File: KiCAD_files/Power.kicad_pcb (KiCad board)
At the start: 4 copper layers, 100 x 100 mm, 206 parts, among them J1 Conn_01x01, J10 Conn_01x01, J101 2604-1102, J102 2604-1102, J103 2604-1102, J104 Conn_01x01, J105 Conn_01x01, J106 Conn_01x01, J107 Conn_01x01, J108 Conn_01x01, J109 Conn_01x01, J110 Conn_01x01, J111 Conn_01x01, J112 Conn_01x01, J113 Conn_01x01, J114 Conn_01x01, J115 Conn_01x01, J116 Conn_01x01, J117 2604-1102, J118 2604-1102, J2 Conn_01x01, J201 Conn_01x01, J202 Conn_01x01, J203 Conn_01x01, J204 Conn_01x01, J205 Conn_01x01, J206 Conn_01x01, J207 Conn_01x01, J208 Conn_01x01, J209 Conn_01x01, J210 Conn_01x01, J3 Conn_01x01, J4 Conn_01x01, J5 Conn_01x01, J6 Conn_01x01, J7 Conn_01x01, J8 Conn_01x01, J9 Conn_01x01, Q1 IPD200N15N3, Q2 IPD200N15N3, Q201 IPD200N15N3, Q202 IPD200N15N3, Q203 IPD200N15N3, Q3 IPD200N15N3, U1 AMC1100DUB, U101 AMC1311, U102 OPA316, U103 OPA316, U104 +-20A, U2 ACS730xLCTR-20AB, U201 AMC1100DUB, U202 ACS730xLCTR-20AB, U203 UCC21222DR, U204 OPA316, U205 OPA316, U206 SFH617A-2X009T, U3 UCC21222DR, U4 OPA316, U5 OPA316, U6 SFH617A-2X009T

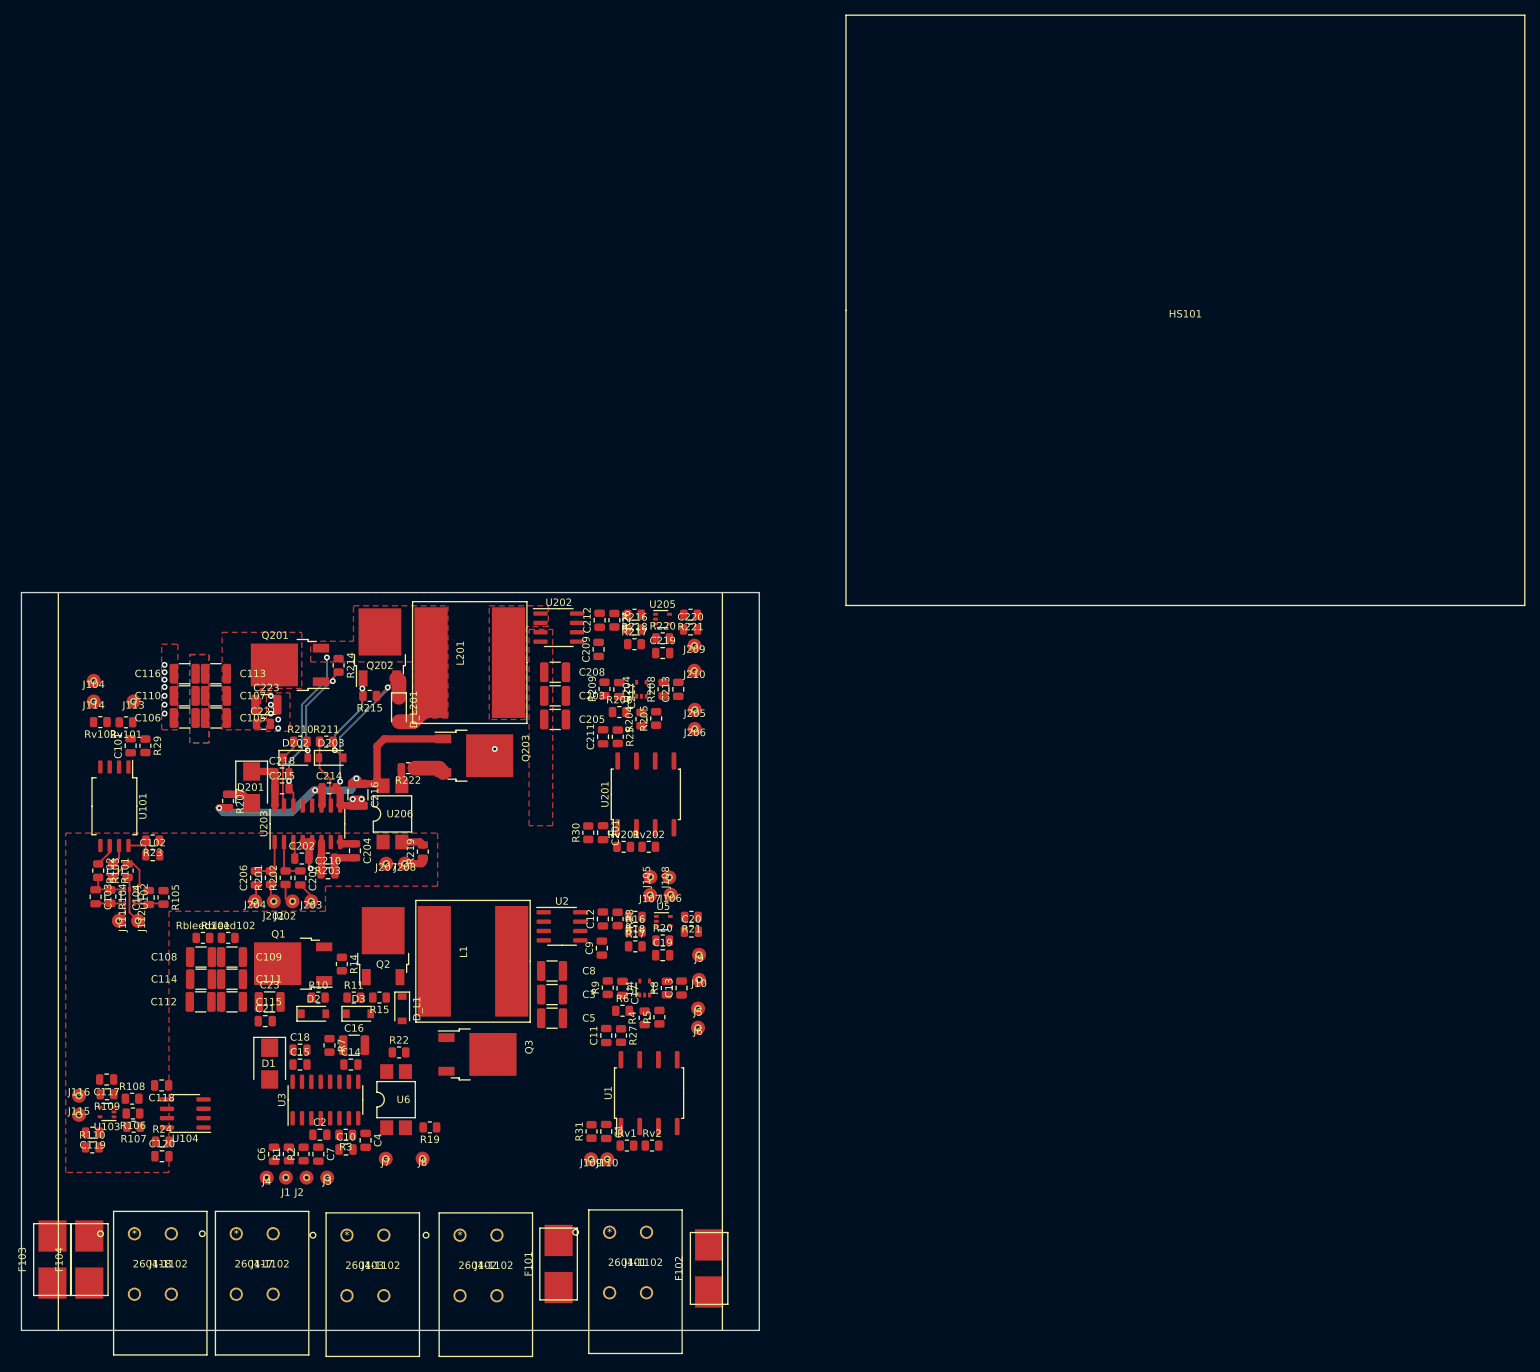
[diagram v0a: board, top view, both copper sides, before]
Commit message: [Power] Finished routing all the tracks, no more rastnet, ready for refining
Former-commit-id: c85419efed005dbd6b325ef0aef7156952f8cebe
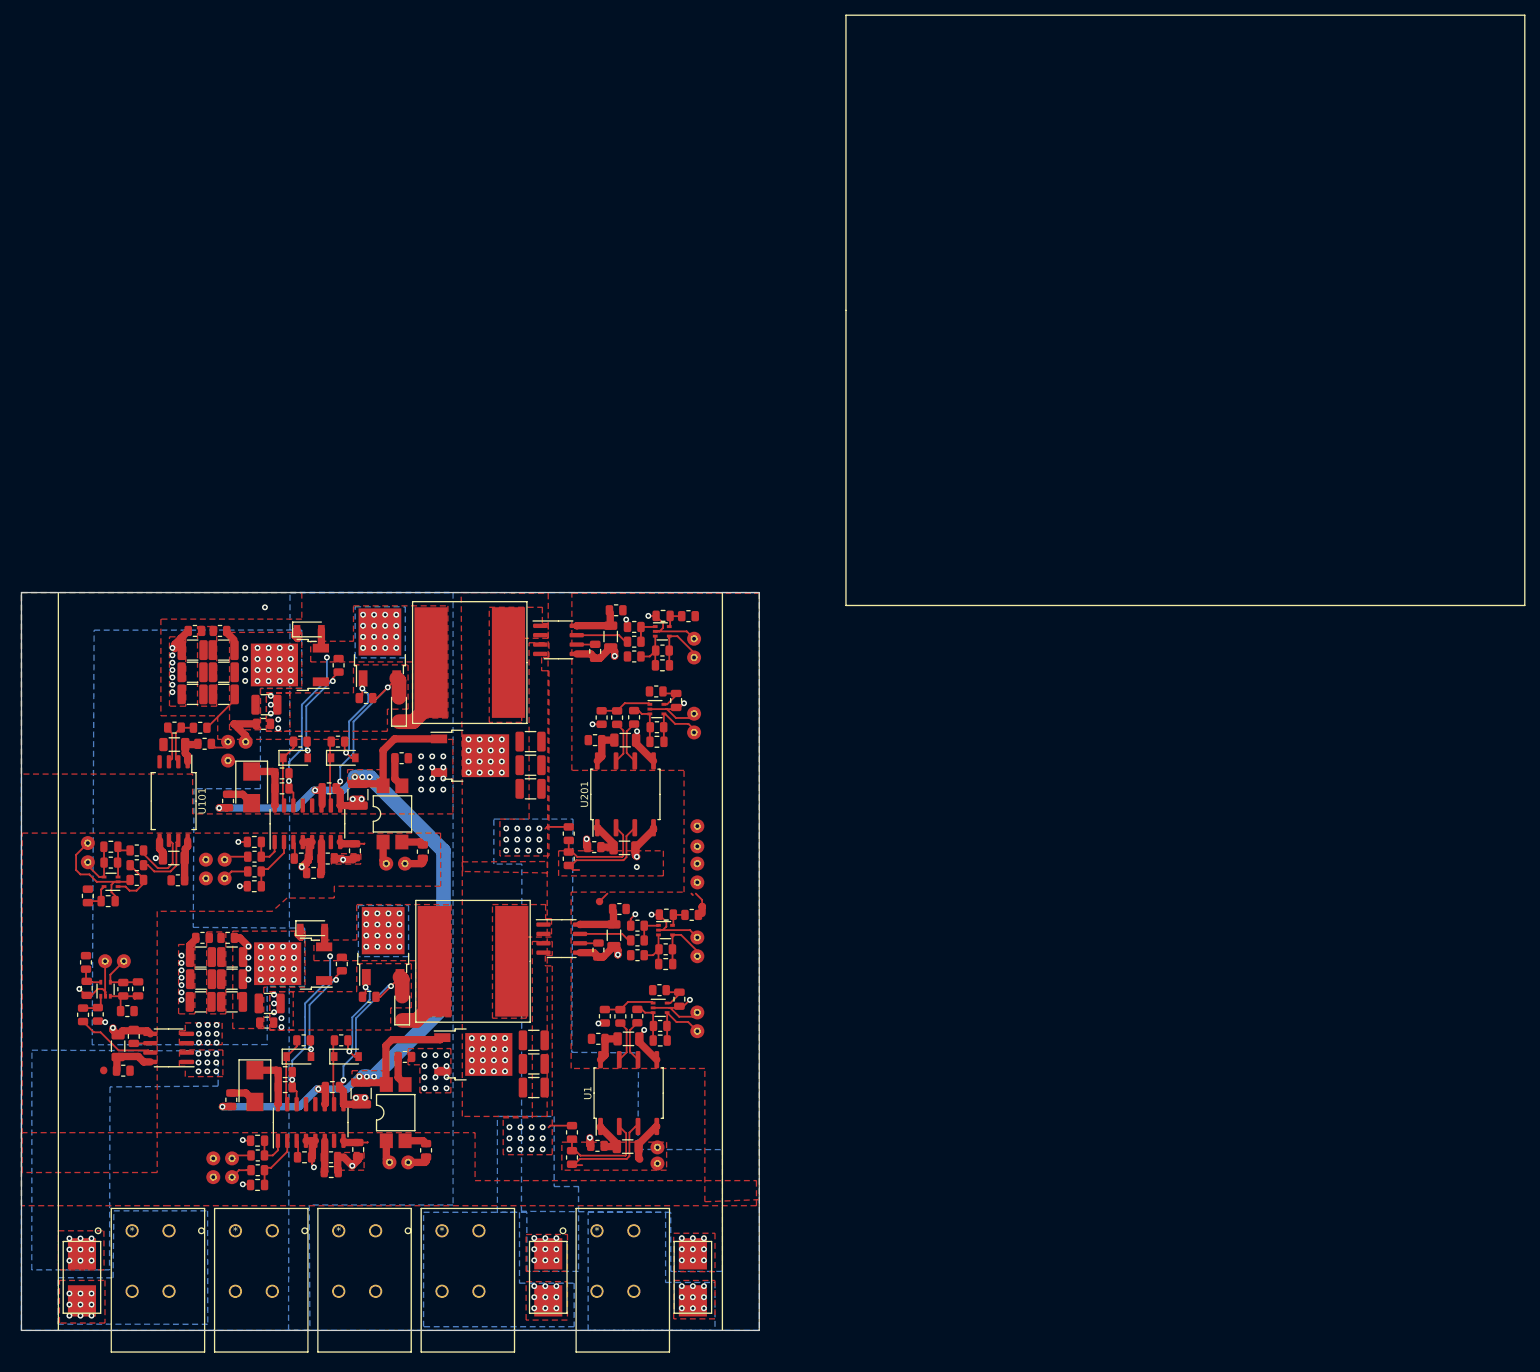
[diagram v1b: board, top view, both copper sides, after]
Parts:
- removed F104: 8A, Footprints:Fuse_holder_omni_blok
- added D_L202: STTH1002CB, Diode_SMD:D_SOD-123, F.Cu at (81.0, 47.0)
- added D_L3: STTH1002CB, Diode_SMD:D_SOD-123, F.Cu at (81.4, 87.5)
- added Rbleed1: 1M, Resistor_SMD:R_0805_2012Metric, F.Cu at (68.9, 47.2)
- added Rbleed2: 1M, Resistor_SMD:R_0805_2012Metric, F.Cu at (65.5, 47.2)
- C1, C101, C102, C11, C12, C120, C201, C211, C212: footprint Capacitor_SMD:C_0805_2012Metric -> Capacitor_SMD:C_1206_3216Metric
- R106, R109, R16, R20, R216, R220: value 62k -> 5.9k
- R107, R108, R17, R18, R217, R218: value 43k -> 20k
- U1, U201: footprint Package_SO:SOP-8_6.62x9.15mm_P2.54mm -> Footprints:SOP-8_6.62x9.15mm_P2.54mm
- U101: footprint Package_SO:SOIC-8_7.5x5.85mm_P1.27mm -> Footprints:SOIC-8_7.5x5.85mm_P1.27mm
- moved C108 41.6 mm to (65.2, 49.8)
- moved C109 41.6 mm to (69.4, 49.8)
- moved C113 38.5 mm to (70.6, 91.4)
- moved C116 38.5 mm to (66.3, 91.4)
- moved R110 25.1 mm to (50.8, 92.1), turned to -90 degrees
- moved J115 21.7 mm to (55.9, 92.0), turned to 90 degrees
- moved J104 20.0 mm to (70.0, 62.2)
- moved J114 19.9 mm to (70.0, 64.8)
- moved C119 19.6 mm to (50.9, 95.6), turned to -90 degrees
- moved J116 18.6 mm to (53.3, 92.0), turned to 90 degrees
- moved U103 16.6 mm to (53.4, 95.8), turned to 90 degrees
- moved C208 16.1 mm to (111.0, 68.6), turned to 180 degrees
- moved J113 16.1 mm to (72.4, 62.2)
- moved C120 16.1 mm to (55.1, 103.5), turned to -90 degrees
- moved C8 16.0 mm to (111.4, 109.1), turned to 180 degrees
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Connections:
- net /Power Leg 1/HRTIM1_CHB1 renamed /Power Leg 1/HRTIM1_CH1
- net /Power Leg 1/HRTIM1_CHB2 renamed /Power Leg 1/HRTIM1_CH2
- net /Power Leg 1/IILow1 renamed /Power Leg 1/IILow
- net /Power Leg 1/VILow1+ renamed /Power Leg 1/VILow+
- net /Power Leg 1/VILow1_op renamed /Power Leg 1/VILow_op
- net /Power Leg 2/HRTIM1_CHB1 renamed /Power Leg 2/HRTIM1_CH1
- net /Power Leg 2/HRTIM1_CHB2 renamed /Power Leg 2/HRTIM1_CH2
- net /Power Leg 2/IILow1 renamed /Power Leg 2/IILow
- net /Power Leg 2/VILow1+ renamed /Power Leg 2/VILow+
- net /Power Leg 2/VILow1_op renamed /Power Leg 2/VILow_op
- C105 pad 1: /Power Leg 1/V_High -> /V_High
- C107 pad 1: /Power Leg 1/V_High -> /V_High
- C109 pad 1: /Power Leg 1/V_High -> /V_High
- C111 pad 1: /Power Leg 1/V_High -> /V_High
- C111 pad 2: Net-(C105-Pad2) -> Net-(C111-Pad2)
- C112 pad 1: Net-(C105-Pad2) -> Net-(C111-Pad2)
- C113 pad 1: /Power Leg 1/V_High -> /V_High
- C113 pad 2: Net-(C105-Pad2) -> Net-(C111-Pad2)
- C114 pad 1: Net-(C105-Pad2) -> Net-(C111-Pad2)
- C115 pad 1: /Power Leg 1/V_High -> /V_High
- C115 pad 2: Net-(C105-Pad2) -> Net-(C111-Pad2)
- C116 pad 1: Net-(C105-Pad2) -> Net-(C111-Pad2)
- C21 pad 1: /Power Leg 1/V_High -> /V_High
- C221 pad 1: /Power Leg 1/V_High -> /V_High
- C223 pad 1: /Power Leg 1/V_High -> /V_High
- C23 pad 1: /Power Leg 1/V_High -> /V_High
- D_L1 pad 1: GNDREF -> /Power Leg 2/SW_Node
- D_L1 pad 2: /Power Leg 2/SW_Node -> GNDREF
- D_L201 pad 1: GNDREF -> /Power Leg 1/SW_Node
- D_L201 pad 2: /Power Leg 1/SW_Node -> GNDREF
- J113 pad 1: /VI_High -> /V_High
- Q1 pad 2: /Power Leg 1/V_High -> /V_High
- Q201 pad 2: /Power Leg 1/V_High -> /V_High
- R107 pad 1: VRef -> +5VD
- R17 pad 1: VRef -> +5VD
- R217 pad 1: VRef -> +5VD
- Rbleed101 pad 1: /Power Leg 1/V_High -> /V_High
- Rbleed101 pad 2: Net-(C105-Pad2) -> Net-(C111-Pad2)
- Rbleed102 pad 1: Net-(C105-Pad2) -> Net-(C111-Pad2)
- Rv101 pad 1: /Power Leg 1/V_High -> /V_High
- U104 pad 3: /Power Leg 1/V_High -> /V_High
- U104 pad 4: /Power Leg 1/V_High -> /V_High
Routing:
- net DGND: track 24.4 -> 140.6 mm, vias 1 -> 22
- net +12V: track 45.3 -> 136.2 mm, vias 3 -> 10
- net VRef: track 0.00 -> 73.6 mm, vias 0 -> 2
- net +5V: track 0.00 -> 67.7 mm, vias 0 -> 2
- net NGND: track 0.00 -> 39.4 mm, vias 1 -> 34
- net GNDREF: track 34.1 -> 72.7 mm, vias 16 -> 57
- net /Power Leg 2/SW_Node: track 0.00 -> 37.0 mm, vias 0 -> 18
- net /V_High: track 0.00 -> 20.1 mm, vias 0 -> 49
- net Net-(D2-Pad2): track 0.00 -> 16.5 mm, vias 0 -> 2
- net Net-(D3-Pad2): track 0.00 -> 16.1 mm, vias 0 -> 2
- net /Power Leg 1/VILow+: track 0.00 -> 13.5 mm
- net /Power Leg 2/VILow+: track 0.00 -> 13.5 mm
- net +5VD: track 4.41 -> 17.4 mm
- net /IIHigh: track 0.00 -> 10.9 mm
- net /Power Leg 2/IILow1_op: track 0.00 -> 9.71 mm
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- added copper zone on F.Cu, net +12V
- added copper zone on F.Cu, net +5VD
- added copper zone on B.Cu, net /Power Leg 1/SW_Node
- added copper zone on B.Cu, net /Power Leg 2/SW_Node
- added copper zone on F.Cu, net /Power Leg 2/SW_Node
- added copper zone on B.Cu, net /V1_Low
- added copper zone on B.Cu, net /V2_Low
- added copper zone on F.Cu, net /V2_Low
- added copper zone on B.Cu, net /VI_High
- added copper zone on F.Cu, net /VI_High
- added copper zone on B.Cu, net /V_High
- added copper zone on F.Cu, net /V_High
- added copper zone on In1.Cu, net DGND
- added copper zone on B.Cu, net GNDREF
- added copper zone on In2.Cu, net GNDREF
- added copper zone on B.Cu, net NGND
- added copper zone on F.Cu, net NGND
- added copper zone on In2.Cu, net NGND
- added copper zone on F.Cu, net Net-(C111-Pad2)
- added copper zone on B.Cu, net Net-(F101-Pad2)
- added copper zone on F.Cu, net Net-(F101-Pad2)
- added copper zone on B.Cu, net Net-(F102-Pad2)
- added copper zone on F.Cu, net Net-(F102-Pad2)
- added copper zone on B.Cu, net Net-(F103-Pad2)
- added copper zone on F.Cu, net Net-(F103-Pad2)
- added copper zone on F.Cu, net Net-(L1-Pad1)
- removed copper zone on F.Cu, net /Power Leg 1/V_High
- removed copper zone on B.Cu, net Net-(C105-Pad2)

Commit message: Supressed backup files
Former-commit-id: af6064aba0445a9773bde6e74b771947025d2895
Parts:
- added H1: MountingHole, MountingHole:MountingHole_3.2mm_M3, F.Cu at (130.6, 114.2)
- added H2: MountingHole, MountingHole:MountingHole_3.2mm_M3, F.Cu at (100.3, 114.0)
- added H3: MountingHole, MountingHole:MountingHole_3.2mm_M3, F.Cu at (100.6, 73.4)
- added H4: MountingHole, MountingHole:MountingHole_3.2mm_M3, F.Cu at (55.2, 73.4)
- added H5: MountingHole, MountingHole:MountingHole_3.2mm_M3, F.Cu at (55.2, 115.4)
- added H6: MountingHole, MountingHole:MountingHole_3.2mm_M3, F.Cu at (130.6, 73.0)
- moved C10 0.50 mm to (83.5, 120.5)
- moved C11 0.50 mm to (123.8, 102.5)
- moved C112 0.50 mm to (65.8, 97.5)
- moved C115 0.50 mm to (70.0, 97.5)
- moved C120 0.50 mm to (54.6, 103.5)
- moved C17 0.50 mm to (130.7, 97.1)
- moved C19 0.50 mm to (128.8, 92.4)
- moved C2 0.50 mm to (79.9, 118.5)
- moved C21 0.50 mm to (74.7, 100.3)
- moved C4 0.50 mm to (87.1, 117.5)
- moved C6 0.50 mm to (73.5, 116.3)
- moved C7 0.50 mm to (73.5, 122.3)
- moved D_L3 0.50 mm to (80.9, 87.5)
- moved J9 0.50 mm to (133.1, 91.3)
- moved Q1 0.50 mm to (78.3, 92.3)
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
